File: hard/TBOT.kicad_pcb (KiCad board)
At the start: 2 copper layers, 99.8 x 54 mm, 58 parts, among them J1 BATTERY, J2 Conn_01x04, J2 R_POWER, J3 L_POWER, J4 OLED_I2C, J5 RTC_I2C, J6 GP_I2C, Q1 ZXMP3A16G, Q2 FDN340P, U1 MPU-6050_Module, U1 TBOT_Motor_Driver_R, U2 TBOT_Motor_Driver_L, U3 INA169, U4 CPR_Encoder_R, U5 CPR_Encoder_L, U6 uA7805, U7 MCP1703A-5002_SOT23, U7 MPU-6050_Module

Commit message: Update with pcb
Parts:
- removed the BZ1 at (-43.0, 89.5)
- removed the BZ1 at (-66.1, 64.2)
- removed C11: 100nF/10V, Capacitor_SMD:C_0805_2012Metric
- removed the C6 at (-66.9, 59.0) (x2)
- removed the C7 at (-66.9, 59.0)
- removed the C7 at (-80.1, 73.2)
- removed the C8 at (-66.9, 59.0) (x2)
- removed C9: 1uF, Capacitor_SMD:C_0805_2012Metric
- removed the J2 at (-66.8, 59.8)
- removed the J2 at (-65.9, 62.0)
- removed the R1 at (-26.6, 70.8)
- removed the R1 at (-66.9, 59.0)
- removed the R2 at (-66.9, 59.0)
- removed the R2 at (-31.0, 70.8)
- removed the R5 at (-66.9, 59.0) (x2)
- removed the R6 at (-66.9, 59.0) (x2)
- removed the U1 at (-66.8, 59.8) (x2)
- removed U3: INA169, Package_TO_SOT_SMD:SOT-23-5
- removed U4: CPR_Encoder_R, TerminalBlock:TerminalBlock_bornier-4_P5.08mm
- removed U5: CPR_Encoder_L, TerminalBlock:TerminalBlock_bornier-4_P5.08mm
- removed U6: uA7805, Package_TO_SOT_SMD:SOT-223
- removed U7: MPU-6050_Module, Connector_PinSocket_2.54mm:PinSocket_1x08_P2.54mm_Vertical
- removed U7: MCP1703A-5002_SOT23, Package_TO_SOT_SMD:SOT-23
- removed XA2: Arduino_Uno_Shield, Arduino_Library:Arduino_Uno_Shield
- added BZ1: Buzzer, Buzzer_Beeper:Buzzer_12x9.5RM7.6, F.Cu at (80.7, 49.5)
- added C6: 100nF/20V, Capacitor_SMD:C_0805_2012Metric, F.Cu at (140.1, 51.1)
- added C7: 100nF/20V, Capacitor_SMD:C_0805_2012Metric, F.Cu at (111.1, 83.8)
- added C8: 100nF/20V, Capacitor_SMD:C_0805_2012Metric, F.Cu at (107.0, 83.8)
- added J10: TBOT_Motor_Driver_R, Connector_PinHeader_2.54mm:PinHeader_1x04_P2.54mm_Vertical, F.Cu at (126.0, 83.0)
- added J11: R_POWER, TerminalBlock_Phoenix:TerminalBlock_Phoenix_MKDS-1,5-2-5.08_1x02_P5.08mm_Horizontal, F.Cu at (157.2, 46.2)
- added J12: CPR_Encoder_R, TerminalBlock_Phoenix:TerminalBlock_Phoenix_MPT-0,5-4-2.54_1x04_P2.54mm_Horizontal, F.Cu at (139.0, 44.7)
- added J2: HC-05 Bluetooth module, Connector_PinSocket_2.54mm:PinSocket_1x04_P2.54mm_Horizontal, F.Cu at (124.1, 68.5)
- added J7: TBOT_Motor_Driver_L, Connector_PinHeader_2.54mm:PinHeader_1x04_P2.54mm_Vertical, F.Cu at (126.0, 42.9)
- added J8: L_POWER, TerminalBlock_Phoenix:TerminalBlock_Phoenix_MKDS-1,5-2-5.08_1x02_P5.08mm_Horizontal, F.Cu at (152.2, 79.7)
- added J9: CPR_Encoder_L, TerminalBlock_Phoenix:TerminalBlock_Phoenix_MPT-0,5-4-2.54_1x04_P2.54mm_Horizontal, F.Cu at (139.0, 81.2)
- added R1: 9.1K, Resistor_SMD:R_0805_2012Metric, F.Cu at (114.7, 82.7)
- added R17: 10k, Resistor_SMD:R_0805_2012Metric, F.Cu at (84.1, 63.6)
- added R2: 3.6K, Resistor_SMD:R_0805_2012Metric, F.Cu at (117.0, 82.7)
- added R5: 0R NI, Resistor_SMD:R_0805_2012Metric, F.Cu at (139.9, 61.1)
- added R6: 100K, Resistor_SMD:R_0805_2012Metric, F.Cu at (147.2, 52.3)
- added SW1: SW_SPDT, Button_Switch_THT:5638A, F.Cu at (138.7, 69.4)
- added U1: INA169, Package_TO_SOT_SMD:SOT-23-5, F.Cu at (136.7, 51.1)
- C1, C2: value 100nF/10V -> 100nF/20V
- C3: value 100nF/10V -> 1uF/20V
- C4: value 10uF/20V -> 0.33uF/20V
- C5: value 0.33uF/20V -> 100nF/20V
- D1: footprint Diode_SMD:D_0805_2012Metric -> Diode_SMD:D_SOD-323
- D2: value BZX384A10Q -> 10V
- J1: footprint TerminalBlock:TerminalBlock_bornier-2_P5.08mm -> TerminalBlock_Phoenix:TerminalBlock_Phoenix_MKDS-1,5-2-5.08_1x02_P5.08mm_Horizontal
- J3: value L_POWER -> MPU-6050_Module; footprint TerminalBlock:TerminalBlock_bornier-2_P5.08mm -> Module:MPU-6050_Module
- Q1: value ZXMP3A16G -> NDT452AP
- R10: value R -> 1K
- R14: value 0R NI -> 10K
- R15: value 10k -> 0R NI
- R8: value 10K -> 0R NI
- R9: value 33k -> 68k
- U2: value TBOT_Motor_Driver_L -> UA78M05IDCY; footprint Connector_PinHeader_2.54mm:PinHeader_1x07_P2.54mm_Vertical -> Package_TO_SOT_SMD:SOT-223
- moved J1 219.7 mm to (155.0, 60.3), turned to -90 degrees
- moved D2 210.5 mm to (143.4, 52.3)
- moved Q1 208.9 mm to (144.7, 58.4), turned to -90 degrees
- moved R7 203.9 mm to (136.9, 54.0), turned to 180 degrees
- moved R9 201.8 mm to (134.6, 48.0), turned to 180 degrees
- moved C3 199.9 mm to (132.9, 51.0), turned to 90 degrees
- moved D1 198.4 mm to (130.5, 79.4)
- moved C4 193.5 mm to (126.6, 55.2), turned to 90 degrees
- moved D3 193.1 mm to (126.2, 62.4), turned to 180 degrees
- moved R10 189.4 mm to (122.5, 62.4)
- moved C1 188.4 mm to (119.9, 83.7)
- moved C5 188.0 mm to (120.8, 48.3), turned to 180 degrees
- moved U2 187.5 mm to (120.6, 53.8), turned to 180 degrees
- moved R11 182.3 mm to (114.5, 41.6)
- moved J3 177.0 mm to (110.3, 45.2), turned to -90 degrees
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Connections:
- net I_MEAS renamed /I_MEAS
- net RX renamed /RX
- net TX renamed /TX
- C1 pad 1: V_BAT_MEAS -> /HW_VERSION
- C1 pad 2: OLED_RST -> GND
- C2 pad 1: HW_VERSION -> /V_BAT_MEAS
- C2 pad 2: OLED_RST -> GND
- C3 pad 1: +5V -> +12V
- C3 pad 2: OLED_RST -> GND
- C4 pad 2: OLED_RST -> GND
- C5 pad 1: +12V -> +5V
- C5 pad 2: OLED_RST -> GND
- D1 pad 1: V_BAT_MEAS -> /V_BAT_MEAS
- D1 pad 2: OLED_RST -> GND
- D3 pad 1: OLED_RST -> GND
- J1 pad 2: OLED_RST -> GND
- J3 pad 1: +12V -> +3V3
- J3 pad 2: OLED_RST -> GND
- J4 pad 2: OLED_RST -> GND
- J4 pad 3: I2C_SCL -> /I2C_SCL
- J4 pad 4: I2C_SDA -> /I2C_SDA
- J4 pad 5: OLED_RST -> /OLED_RST
- J5 pad 1: I2C_SCL -> /I2C_SCL
- J5 pad 2: I2C_SDA -> /I2C_SDA
- J5 pad 3: unconnected-(J5-Pad3) -> +3V3
- J5 pad 4: OLED_RST -> GND
- J6 pad 2: OLED_RST -> GND
- J6 pad 3: I2C_SCL -> /I2C_SCL
- J6 pad 4: I2C_SDA -> /I2C_SDA
- Q1 pad 2: Net-(Q1-Pad2) -> /D
- R11 pad 1: +12V -> Net-(R11-Pad1)
- R11 pad 2: Net-(R11-Pad2) -> /R_ENCODER_B
- R12 pad 2: R_ENCODER_A -> /L_ENCODER_B
- R13 pad 2: R_ENCODER_B -> /BUZZER
- R14 pad 1: Net-(R14-Pad1) -> /BUZZER
- R14 pad 2: /BUZZER -> Net-(Q2-Pad1)
- R15 pad 1: +3V3 -> /BUZZER
- R15 pad 2: I2C_SDA -> Net-(BZ1-Pad1)
- R16 pad 2: I2C_SCL -> /I2C_SDA
- R3 pad 1: +5V -> V_BAT
- R3 pad 2: HW_VERSION -> /V_BAT_MEAS
- R4 pad 1: HW_VERSION -> /V_BAT_MEAS
- R4 pad 2: OLED_RST -> GND
- R8 pad 1: /BUZZER -> +12V
- R8 pad 2: Net-(Q2-Pad1) -> VDD
- R9 pad 2: OLED_RST -> GND
- U2 pad 1: unconnected-(U2-Pad1) -> +12V
- U2 pad 2: OLED_RST -> GND
- U2 pad 3: M_EN -> +5V
- U2 pad 4: L_FORWARD -> GND
- XA1 pad A0: HW_VERSION -> /HW_VERSION
- XA1 pad A1: V_BAT_MEAS -> /V_BAT_MEAS
- XA1 pad D10: L_ENCODER_B -> Net-(R12-Pad1)
- XA1 pad D11: Net-(R14-Pad1) -> Net-(R13-Pad1)
- XA1 pad D12: M_EN -> /M_EN
- XA1 pad D18: L_ENCODER_B -> /L_ENCODER_B
- XA1 pad D19: R_ENCODER_B -> /R_ENCODER_B
- XA1 pad D2: L_FORWARD -> /L_FORWARD
- XA1 pad D20: I2C_SDA -> unconnected-(XA1-PadD20)
- XA1 pad D21: I2C_SCL -> unconnected-(XA1-PadD21)
- XA1 pad D3: L_REVERSE -> /L_REVERSE
- XA1 pad D4: L_ENCODER_A -> /L_ENCODER_A
- XA1 pad D5: Net-(R12-Pad1) -> /R_ENCODER_A
- XA1 pad D6: R_REVERSE -> /R_REVERSE
- XA1 pad D7: Net-(R13-Pad1) -> Net-(R11-Pad1)
- XA1 pad D8: R_FORWARD -> /R_FORWARD
- XA1 pad D9: OLED_RST -> /OLED_RST
- XA1 pad GND1: OLED_RST -> GND
- XA1 pad GND2: OLED_RST -> GND
- XA1 pad GND3: OLED_RST -> GND
- XA1 pad GND5: OLED_RST -> GND
- XA1 pad GND6: OLED_RST -> GND
- XA1 pad SCL: unconnected-(XA1-PadSCL) -> /I2C_SCL
- XA1 pad SDA: unconnected-(XA1-PadSDA) -> /I2C_SDA
- XA1 pad VIN: Net-(R11-Pad2) -> VDD
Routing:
- net +5V: track 0.00 -> 181.1 mm, vias 0 -> 11
- net +3V3: track 0.00 -> 163.2 mm, vias 0 -> 10
- net +12V: track 0.00 -> 122.2 mm, vias 0 -> 6
- net /L_ENCODER_B: track 0.00 -> 119.0 mm, vias 0 -> 6
- net /BUZZER: track 0.00 -> 99.0 mm, vias 0 -> 2
- net /I2C_SCL: track 0.00 -> 93.1 mm, vias 0 -> 7
- net /I2C_SDA: track 0.00 -> 86.1 mm, vias 0 -> 6
- net /M_EN: track 0.00 -> 72.8 mm, vias 0 -> 2
- net /L_ENCODER_A: track 0.00 -> 69.3 mm, vias 0 -> 2
- net /R_FORWARD: track 0.00 -> 62.8 mm, vias 0 -> 4
- net /R_REVERSE: track 0.00 -> 58.8 mm, vias 0 -> 2
- net /I_MEAS: track 0.00 -> 54.2 mm, vias 0 -> 3
- net /R_ENCODER_B: track 0.00 -> 49.7 mm, vias 0 -> 6
- net /OLED_RST: track 0.00 -> 48.2 mm, vias 0 -> 3
- net V_BAT: track 0.00 -> 43.6 mm, vias 0 -> 4
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- added copper zone on B.Cu, net GND
- added copper zone on F.Cu, net GND
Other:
- board size 99.8 x 54 mm -> 99.4 x 53.7 mm

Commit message: DRC checked
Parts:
- moved R16 3.95 mm to (83.7, 62.0)
- moved R17 3.73 mm to (83.7, 59.9)
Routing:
- net +12V: track 122.2 -> 126.3 mm, vias 6 -> 5
- net +3V3: track 163.2 -> 166.0 mm, vias 10 -> 9
- net /I2C_SCL: track 93.1 -> 92.3 mm
- net VDD: track 7.57 -> 7.02 mm
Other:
- board size 99.4 x 53.7 mm -> 101.8 x 53.5 mm

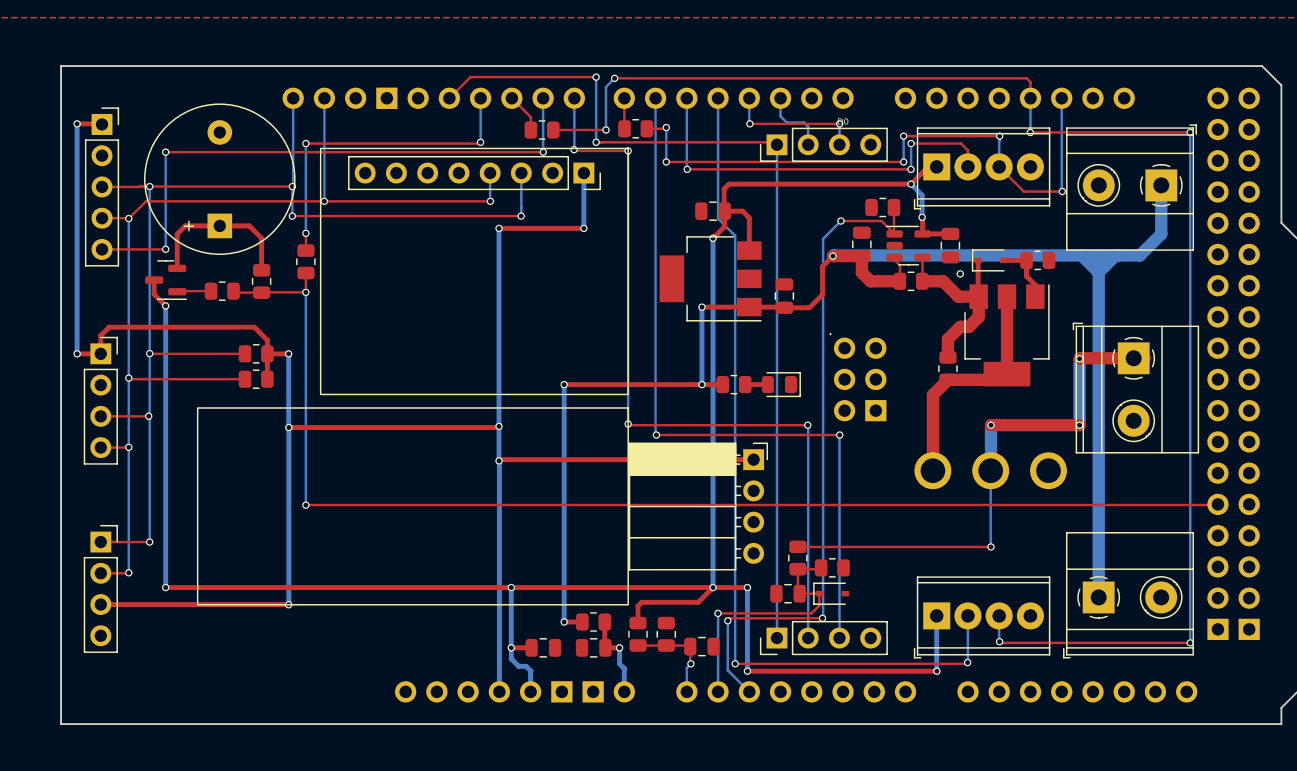
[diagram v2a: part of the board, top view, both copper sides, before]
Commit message: Add jumper for Bluetooth selection
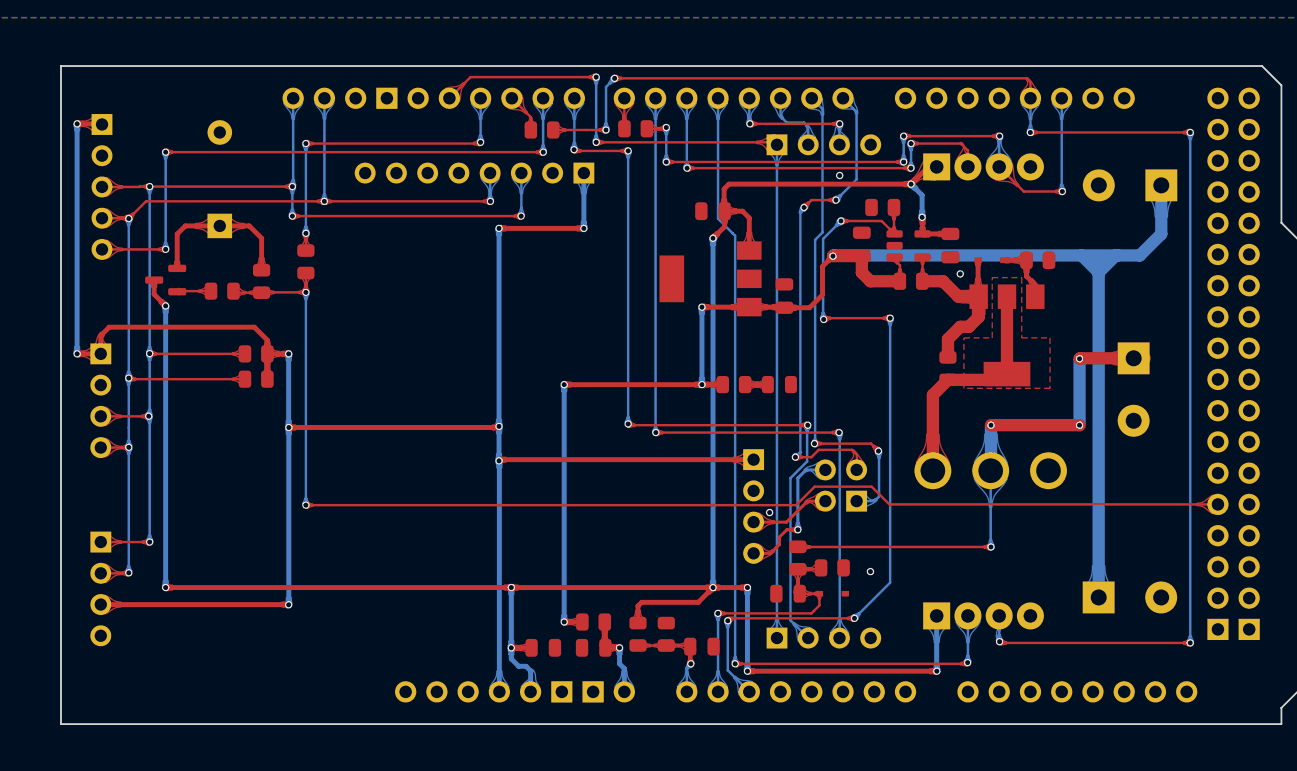
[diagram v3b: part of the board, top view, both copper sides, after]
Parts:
- added JP1: Jumper_4_Open, Connector_PinHeader_2.54mm:PinHeader_2x02_P2.54mm_Vertical, F.Cu at (132.5, 71.9)
- renumbered R8 to R7, R7 to R8
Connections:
- J2 pad 3: /BLE_RX -> /BLUETOOTH_TX
- J2 pad 4: /BLE_TX -> /BLUETOOTH_RX
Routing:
- net /TX: track 0.00 -> 39.8 mm, vias 0 -> 2
- net /RX: track 0.00 -> 39.5 mm, vias 0 -> 3
- net /BLUETOOTH_RX: track 0.00 -> 11.5 mm, vias 0 -> 1
- net /I_MEAS: track 54.2 -> 63.5 mm, vias 3 -> 5
- net /BLUETOOTH_TX: track 0.00 -> 6.54 mm
- net /BUZZER: track 99.0 -> 100.3 mm
- net /R_FORWARD: track 62.8 -> 63.9 mm
- net GND: vias 1 -> 4
- added copper zone on F.Cu, net /D

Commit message: First version of TBOT hardware
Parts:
- Q2: value FDN340P -> DMN2050L
- R1: value 9.1K -> 0R
- R2: value 3.6K -> 0R NI
- moved J12 7.63 mm to (146.6, 44.7), turned to 180 degrees
- moved J1 5.09 mm to (155.1, 65.3), turned to 90 degrees
- moved C4 0.35 mm to (127.0, 55.2)
- moved C6 0.23 mm to (140.3, 51.1)
- moved Q2 0.11 mm to (76.2, 53.9)
- renumbered R7 to R10, R15 to R14, R14 to R15, R8 to R7, R9 to R8, R10 to R9
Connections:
- net +3V3 renamed +3.3V
- BZ1 pad 1: Net-(BZ1-Pad1) -> +5V
- BZ1 pad 2: GND -> Net-(BZ1-Pad2)
- JP1 pad 1: /TX -> /RX
- JP1 pad 3: /RX -> /TX
- Q2 pad 2: Net-(BZ1-Pad1) -> GND
- Q2 pad 3: +5V -> Net-(BZ1-Pad2)
- R14 pad 2: Net-(BZ1-Pad1) -> +5V
- U2 pad 4: GND -> (no net)
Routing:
- net +5V: track 181.1 -> 201.3 mm, vias 11 -> 12
- net Net-(BZ1-Pad2): track 0.00 -> 16.1 mm, vias 0 -> 1
- net Net-(BZ1-Pad1): track 12.9 -> 0.00 mm
- net V_BAT: track 43.5 -> 34.8 mm, vias 4 -> 1
- net /RX: track 39.5 -> 44.3 mm, vias 3 -> 4
- net /TX: track 39.8 -> 36.6 mm, vias 2 -> 1
- net +3.3V: track 166.0 -> 163.4 mm
- net /R_ENCODER_A: track 32.3 -> 34.7 mm
- net /M_EN: track 73.2 -> 71.8 mm
- net /I2C_SCL: track 92.3 -> 91.0 mm
- net /L_ENCODER_B: track 119.0 -> 117.7 mm
- net /R_ENCODER_B: track 49.7 -> 50.7 mm, vias 6 -> 4
- net /I_MEAS: track 63.5 -> 62.5 mm
- net /L_REVERSE: track 11.1 -> 10.2 mm, vias 2 -> 0
- net /L_ENCODER_A: track 69.3 -> 68.5 mm
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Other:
- board text added: "B_RX"
- board text added: "B_TX"
- board text added: "Battery"
- board text added: "GND"
- board text added: "HC-05 Bluetooth module"
- board text added: "I2C"
- board text added: "Left driver"
- board text added: "Left encoder"
- board text added: "Left power"
- board text added: "MPU-6050 Module"
- board text added: "Oled"
- board text added: "RTC"
- board text added: "RX"
- board text added: "Right driver"
- board text added: "Right encoder"
- board text added: "Right power"
- board text added: "TBOT shield for arduino v1 T.Jenny T.Ateba"
- board text added: "TX"
- board text added: "V+"
